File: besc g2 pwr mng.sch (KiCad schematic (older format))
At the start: 47 parts, among them IC1 LTC7801, J17 12V OUT, Q25 FDMS86252L, Q26 BSC110N15NS5, U11 R-78E5.0-0.5, U12 LP5907MFX-3.3

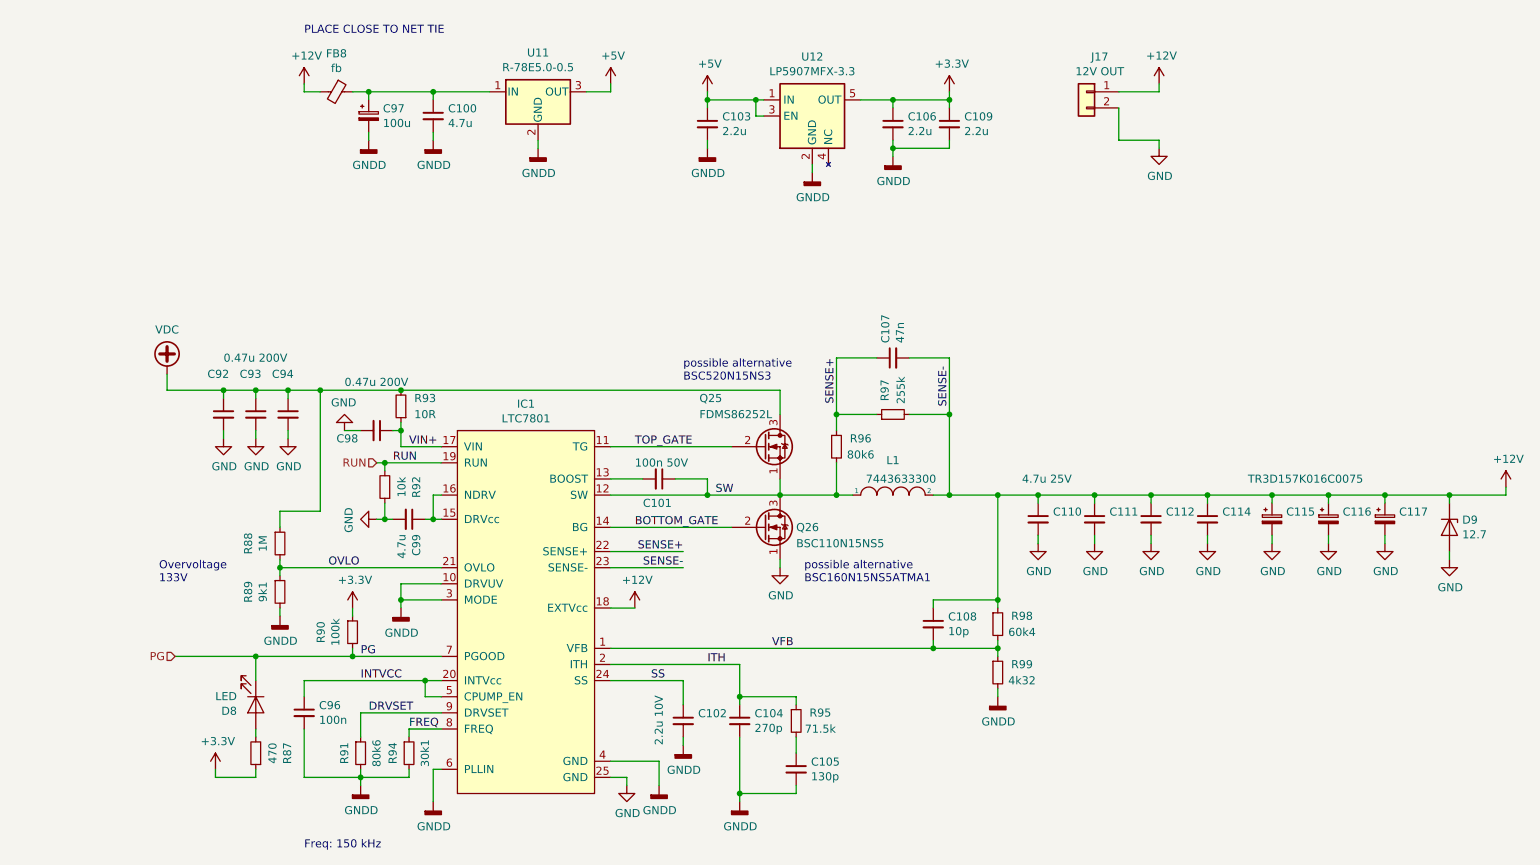
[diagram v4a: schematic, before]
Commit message: finished routing, added bom and step
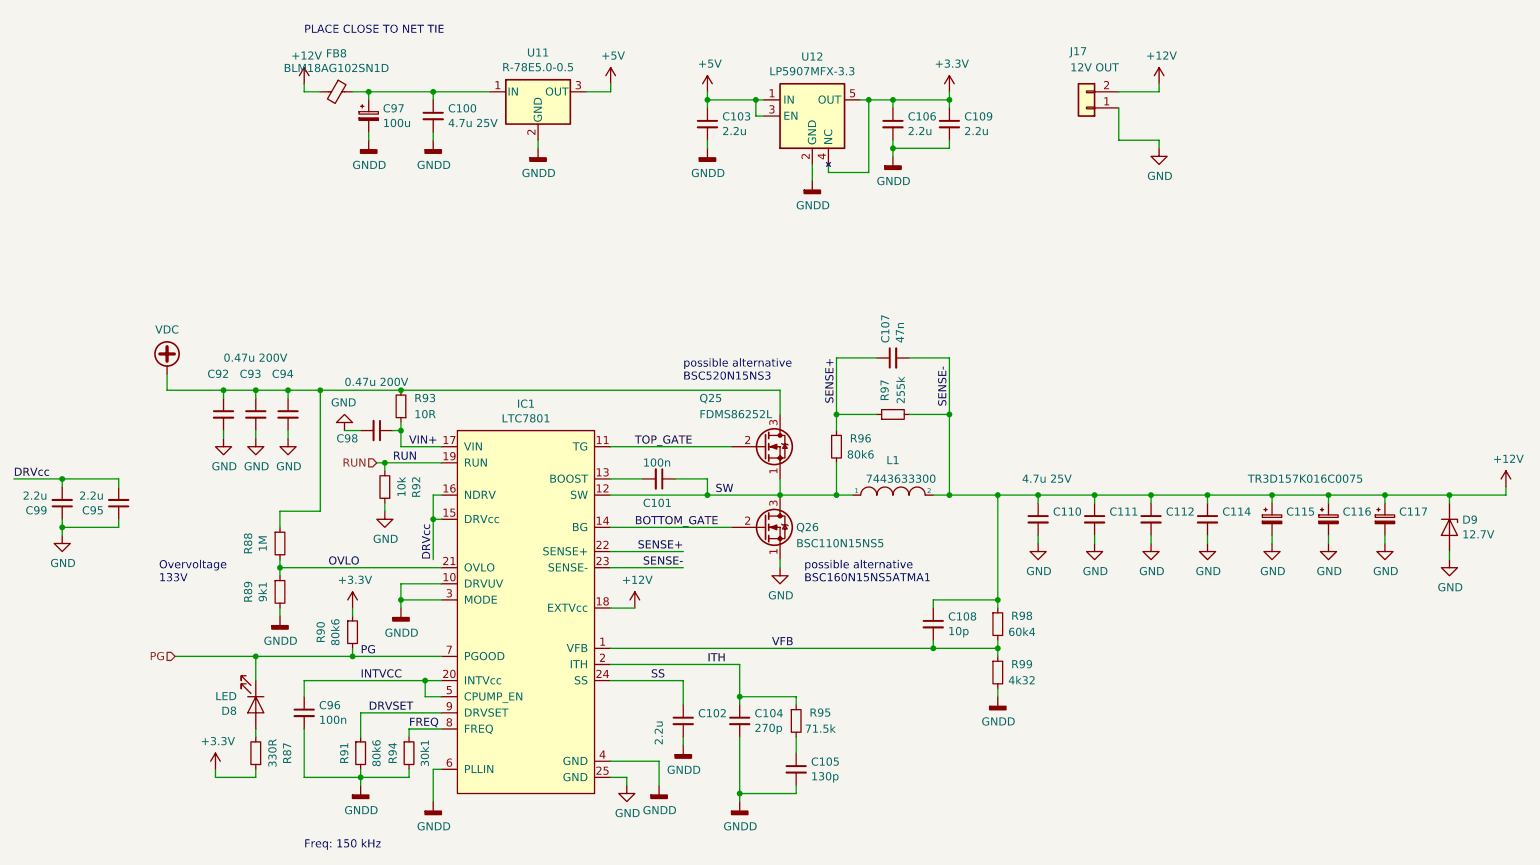
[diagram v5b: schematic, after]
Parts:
- added C95: 2.2u, Capacitor_SMD:C_0603_1608Metric, symbol Device:C_Small
- C100: value 4.7u -> 4.7u 25V
- C101: value 100n 50V -> 100n
- C102: value 2.2u 10V -> 2.2u
- C92, C93, C94, C98: footprint Capacitor_SMD:C_1206_3216Metric -> Capacitor_SMD:C_1210_3225Metric
- C99: value 4.7u -> 2.2u
- D9: value 12.7 -> 12.7V
- FB8: value fb -> BLM18AG102SN1D
- R87: value 470 -> 330R
- R90: value 100k -> 80k6
- R93: footprint Resistor_SMD:R_0603_1608Metric -> Resistor_SMD:R_0805_2012Metric
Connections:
- net +12V: now also J17.2 (Pin_2); no longer J17.1 (Pin_1)
- net +3V3: now also U12.4 (NC)
- net GND: now also C99.1, J17.1 (Pin_1), C95.1; no longer C99.2, J17.2 (Pin_2)
- net DRVcc: now reaches IC1.15 (DRVcc), IC1.16 (NDRV)
- net DRVcc: now also C99.2, C95.2; no longer C99.1
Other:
- moved on the sheet: C99
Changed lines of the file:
@@
 encoding utf-8
 Sheet 5 5
-Title ""
-Date ""
-Rev ""
-Comp ""
+Title "BESC Gen 2"
+Date "14.7.2019"
+Rev "init"
+Comp "e.pavlin.si"
 Comment1 ""
 Comment2 ""
@@
 P 3300 1600
 F 0 "FB8" V 3063 1600 50  0000 C CNN
-F 1 "fb" V 3154 1600 50  0000 C CNN
+F 1 "BLM18AG102SN1D" V 3154 1600 50  0000 C CNN
 F 2 "Inductor_SMD:L_0603_1608Metric" V 3230 1600 50  0001 C CNN
 F 3 "~" H 3300 1600 50  0001 C CNN
@@
 P 3900 1750
 F 0 "C100" H 3992 1796 50  0000 L CNN
-F 1 "4.7u" H 3992 1705 50  0000 L CNN
+F 1 "4.7u 25V" H 3992 1705 50  0000 L CNN
 F 2 "Capacitor_SMD:C_1206_3216Metric" H 3900 1750 50  0001 C CNN
 F 3 "~" H 3900 1750 50  0001 C CNN
@@
 L power:GNDD #PWR0154
 U 1 1 5DBF730C
-P 6250 2100
-F 0 "#PWR0154" H 6250 1850 50  0001 C CNN
-F 1 "GNDD" H 6254 1945 50  0000 C CNN
-F 2 "" H 6250 2100 50  0001 C CNN
-F 3 "" H 6250 2100 50  0001 C CNN
-	1    6250 2100
-	1    0    0    -1
-$EndComp
-Wire Wire Line
-	6250 2050 6250 2100
+P 6250 2150
+F 0 "#PWR0154" H 6250 1900 50  0001 C CNN
+F 1 "GNDD" H 6254 1995 50  0000 C CNN
+F 2 "" H 6250 2150 50  0001 C CNN
+F 3 "" H 6250 2150 50  0001 C CNN
+	1    6250 2150
+	1    0    0    -1
+$EndComp
 Wire Wire Line
 	5950 1650 5900 1650
@@
 	5600 1900 5600 1950
 Wire Wire Line
-	6550 1650 6750 1650
+	6550 1650 6600 1650
 Wire Wire Line
 	7100 1650 7100 1700
@@
 L Connector_Generic:Conn_01x02 J17
 U 1 1 5DC09E1F
-P 7950 1600
-F 0 "J17" H 7868 1817 50  0000 C CNN
-F 1 "12V OUT" H 7868 1726 50  0000 C CNN
-F 2 "conn-amass:AMASS_XT30U-M_1x02_P5.0mm_Vertical" H 7950 1600 50  0001 C CNN
-F 3 "~" H 7950 1600 50  0001 C CNN
-	1    7950 1600
-	-1   0    0    -1
+P 7950 1700
+F 0 "J17" H 8000 1350 50  0000 C CNN
+F 1 "12V OUT" H 7900 1450 50  0000 C CNN
+F 2 "conn-amass:AMASS_XT30U-M_1x02_P5.0mm_Vertical" H 7950 1700 50  0001 C CNN
+F 3 "~" H 7950 1700 50  0001 C CNN
+	1    7950 1700
+	-1   0    0    1
 $EndComp
 Wire Wire Line
@@
 AR Path="/5DBE359C/5CDAF81D" Ref="R90"  Part="1"
 F 0 "R90" V 3204 4950 50  0000 C CNN
-F 1 "100k" V 3295 4950 50  0000 C CNN
+F 1 "80k6" V 3295 4950 50  0000 C CNN
 F 2 "Resistor_SMD:R_0603_1608Metric" H 3400 4950 50  0001 C CNN
 F 3 "~" H 3400 4950 50  0001 C CNN
@@
 	5100 5850 5100 5900
 $Comp
-L Device:C_Small C102
-U 1 1 5CDAF866
-P 5450 5500
-F 0 "C102" H 5542 5546 50  0000 L CNN
-F 1 "2.2u 10V" V 5300 5350 50  0000 L CNN
-F 2 "Capacitor_SMD:C_0603_1608Metric" H 5450 5500 50  0001 C CNN
-F 3 "~" H 5450 5500 50  0001 C CNN
-	1    5450 5500
-	1    0    0    -1
-$EndComp
-$Comp
 L Device:C_Small C104
 U 1 1 5CDAF86C
@@
 P 5300 4000
 F 0 "C101" V 5450 3900 50  0000 L CNN
-F 1 "100n 50V" V 5200 3850 50  0000 L CNN
+F 1 "100n" V 5200 3900 50  0000 L CNN
 F 2 "Capacitor_SMD:C_0603_1608Metric" H 5300 4000 50  0001 C CNN
 F 3 "~" H 5300 4000 50  0001 C CNN
@@
 L power:GND #PWR0140
 U 1 1 5CDAF8D2
-P 3550 4250
-F 0 "#PWR0140" H 3550 4000 50  0001 C CNN
-F 1 "GND" H 3555 4077 50  0000 C CNN
-F 2 "" H 3550 4250 50  0001 C CNN
-F 3 "" H 3550 4250 50  0001 C CNN
-	1    3550 4250
-	0    1    1    0
-$EndComp
-Wire Wire Line
-	3650 4250 3600 4250
-Wire Wire Line
-	3850 4250 3900 4250
+P 3600 4200
+F 0 "#PWR0140" H 3600 3950 50  0001 C CNN
+F 1 "GND" H 3605 4027 50  0000 C CNN
+F 2 "" H 3600 4200 50  0001 C CNN
+F 3 "" H 3600 4200 50  0001 C CNN
+	1    3600 4200
+	1    0    0    -1
+$EndComp
 Wire Wire Line
 	3900 4100 3900 4250
-Connection ~ 3900 4250
 Wire Wire Line
 	3900 4250 3950 4250
@@
 F 0 "C92" H 2500 3850 50  0000 L CNN
 F 1 "0.47u 200V" H 2600 3950 50  0000 L CNN
-F 2 "Capacitor_SMD:C_1206_3216Metric" H 2600 3600 50  0001 C CNN
+F 2 "Capacitor_SMD:C_1210_3225Metric" H 2600 3600 50  0001 C CNN
 F 3 "~" H 2600 3600 50  0001 C CNN
 	1    2600 3600
@@
 L Device:C_Small C99
 U 1 1 5CDAF8E4
-P 3750 4250
-F 0 "C99" H 3842 4296 50  0000 L CNN
-F 1 "4.7u" H 3842 4205 50  0000 L CNN
-F 2 "Capacitor_SMD:C_0603_1608Metric" H 3750 4250 50  0001 C CNN
-F 3 "~" H 3750 4250 50  0001 C CNN
-	1    3750 4250
-	0    1    1    0
+P 1600 4150
+F 0 "C99" H 1692 4196 50  0000 L CNN
+F 1 "2.2u" H 1692 4105 50  0000 L CNN
+F 2 "Capacitor_SMD:C_0603_1608Metric" H 1600 4150 50  0001 C CNN
+F 3 "~" H 1600 4150 50  0001 C CNN
+	1    1600 4150
+	-1   0    0    1
 $EndComp
 $Comp
@@
 F 0 "C93" H 2700 3850 50  0000 L CNN
 F 1 "0.47u 200V" H 2892 3555 50  0001 L CNN
-F 2 "Capacitor_SMD:C_1206_3216Metric" H 2800 3600 50  0001 C CNN
+F 2 "Capacitor_SMD:C_1210_3225Metric" H 2800 3600 50  0001 C CNN
 F 3 "~" H 2800 3600 50  0001 C CNN
 	1    2800 3600
@@
 F 0 "C94" H 2900 3850 50  0000 L CNN
 F 1 "0.47u 200V" H 3092 3555 50  0001 L CNN
-F 2 "Capacitor_SMD:C_1206_3216Metric" H 3000 3600 50  0001 C CNN
+F 2 "Capacitor_SMD:C_1210_3225Metric" H 3000 3600 50  0001 C CNN
 F 3 "~" H 3000 3600 50  0001 C CNN
 	1    3000 3600
@@
 F 0 "R93" H 3550 3500 50  0000 C CNN
 F 1 "10R" H 3550 3600 50  0000 C CNN
-F 2 "Resistor_SMD:R_0603_1608Metric" H 3700 3550 50  0001 C CNN
+F 2 "Resistor_SMD:R_0805_2012Metric" H 3700 3550 50  0001 C CNN
 F 3 "~" H 3700 3550 50  0001 C CNN
 	1    3700 3550
@@
 F 0 "C98" V 3600 3450 50  0000 L CNN
 F 1 "0.47u 200V" V 3250 3500 50  0000 L CNN
-F 2 "Capacitor_SMD:C_1206_3216Metric" H 3550 3700 50  0001 C CNN
+F 2 "Capacitor_SMD:C_1210_3225Metric" H 3550 3700 50  0001 C CNN
 F 3 "~" H 3550 3700 50  0001 C CNN
 	1    3550 3700
@@
 $EndComp
 Wire Wire Line
-	3600 4150 3600 4250
-Connection ~ 3600 4250
-Wire Wire Line
-	3600 4250 3550 4250
+	3600 4150 3600 4200
 Wire Wire Line
 	3550 3900 3600 3900
@@
 AR Path="/5DBE359C/5CDAF96E" Ref="R87"  Part="1"
 F 0 "R87" V 2604 5700 50  0000 C CNN
-F 1 "470" V 2695 5700 50  0000 C CNN
+F 1 "330R" V 2695 5700 50  0000 C CNN
 F 2 "Resistor_SMD:R_0603_1608Metric" H 2800 5700 50  0001 C CNN
 F 3 "~" H 2800 5700 50  0001 C CNN
@@
 P 10200 4300
 F 0 "D9" V 10154 4379 50  0000 L CNN
-F 1 "12.7" V 10245 4379 50  0000 L CNN
+F 1 "12.7V" V 10245 4379 50  0000 L CNN
 F 2 "Diode_SMD:D_SMA" H 10200 4300 50  0001 C CNN
 F 3 "~" H 10200 4300 50  0001 C CNN
@@
 Wire Wire Line
 	3900 1600 4250 1600
+Wire Wire Line
+	6250 2050 6250 2150
+Wire Wire Line
+	6350 2100 6350 2050
+Connection ~ 6600 1650
+Wire Wire Line
+	6600 1650 6750 1650
+Wire Wire Line
+	6600 2100 6600 1650
+Wire Wire Line
+	6350 2100 6600 2100
+$Comp
+L Device:C_Small C102
+U 1 1 5CDAF866
+P 5450 5500
+F 0 "C102" H 5542 5546 50  0000 L CNN
+F 1 "2.2u" V 5300 5350 50  0000 L CNN
+F 2 "Capacitor_SMD:C_0603_1608Metric" H 5450 5500 50  0001 C CNN
+F 3 "~" H 5450 5500 50  0001 C CNN
+	1    5450 5500
+	1    0    0    -1
+$EndComp
+Text Label 3900 4500 1    50   ~ 0
+DRVcc
+Wire Wire Line
+	3900 4250 3900 4500
+Connection ~ 3900 4250
+Text Label 1300 4000 0    50   ~ 0
+DRVcc
+$Comp
+L Device:C_Small C95
+U 1 1 5D624C95
+P 1950 4150
+F 0 "C95" H 2042 4196 50  0000 L CNN
+F 1 "2.2u" H 2042 4105 50  0000 L CNN
+F 2 "Capacitor_SMD:C_0603_1608Metric" H 1950 4150 50  0001 C CNN
+F 3 "~" H 1950 4150 50  0001 C CNN
+	1    1950 4150
+	-1   0    0    1
+$EndComp
+Wire Wire Line
+	1950 4000 1950 4050
+Wire Wire Line
+	1600 4050 1600 4000
+Connection ~ 1600 4000
+Wire Wire Line
+	1600 4000 1950 4000
+Wire Wire Line
+	1300 4000 1600 4000
+$Comp
+L power:GND #PWR04
+U 1 1 5D642885
+P 1600 4350
+F 0 "#PWR04" H 1600 4100 50  0001 C CNN
+F 1 "GND" H 1605 4177 50  0000 C CNN
+F 2 "" H 1600 4350 50  0001 C CNN
+F 3 "" H 1600 4350 50  0001 C CNN
+	1    1600 4350
+	1    0    0    -1
+$EndComp
+Wire Wire Line
+	1600 4250 1600 4300
+Wire Wire Line
+	1600 4300 1950 4300
+Wire Wire Line
+	1950 4300 1950 4250
+Connection ~ 1600 4300
+Wire Wire Line
+	1600 4300 1600 4350
 $EndSCHEMATC

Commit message: added assembly drawing
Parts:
- U12: symbol Regulator_Linear:LP5907MFX-3.3 -> besc-g2-rescue:LP5907MFX-3.3-Regulator_Linear
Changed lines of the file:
@@
 	5000 1600 5000 1550
 $Comp
-L Regulator_Linear:LP5907MFX-3.3 U12
+L besc-g2-rescue:LP5907MFX-3.3-Regulator_Linear U12
 U 1 1 5DBF5F54
 P 6250 1750
+AR Path="/5DBF5F54" Ref="U12"  Part="1"
+AR Path="/5DBE359C/5DBF5F54" Ref="U12"  Part="1"
 F 0 "U12" H 6250 2117 50  0000 C CNN
 F 1 "LP5907MFX-3.3" H 6250 2026 50  0000 C CNN

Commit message: fixed schematic, added firmware files
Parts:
- IC1: symbol moje:LTC7801 -> besc-g2-rescue:LTC7801-moje
- U12: symbol besc-g2-rescue:LP5907MFX-3.3-Regulator_Linear -> besc-g2-rescue:LP5907MFX-3.3-Regulator_Linear-besc-g2-rescue
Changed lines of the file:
@@
 	5000 1600 5000 1550
 $Comp
-L besc-g2-rescue:LP5907MFX-3.3-Regulator_Linear U12
+L besc-g2-rescue:LP5907MFX-3.3-Regulator_Linear-besc-g2-rescue U12
 U 1 1 5DBF5F54
 P 6250 1750
@@
 $EndComp
 $Comp
-L moje:LTC7801 IC1
+L besc-g2-rescue:LTC7801-moje IC1
 U 1 1 5CDAFA6C
 P 4500 4850
